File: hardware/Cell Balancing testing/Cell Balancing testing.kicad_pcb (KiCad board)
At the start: 2 copper layers, 27.9 x 48.8 mm, 29 parts, among them J1 pwm, J2 cell, U1 2PD2150-QX, U2 2PD2150-QX, U3 2PD2150-QX, U4 2PD2150-QX, U5 DMN62D0U

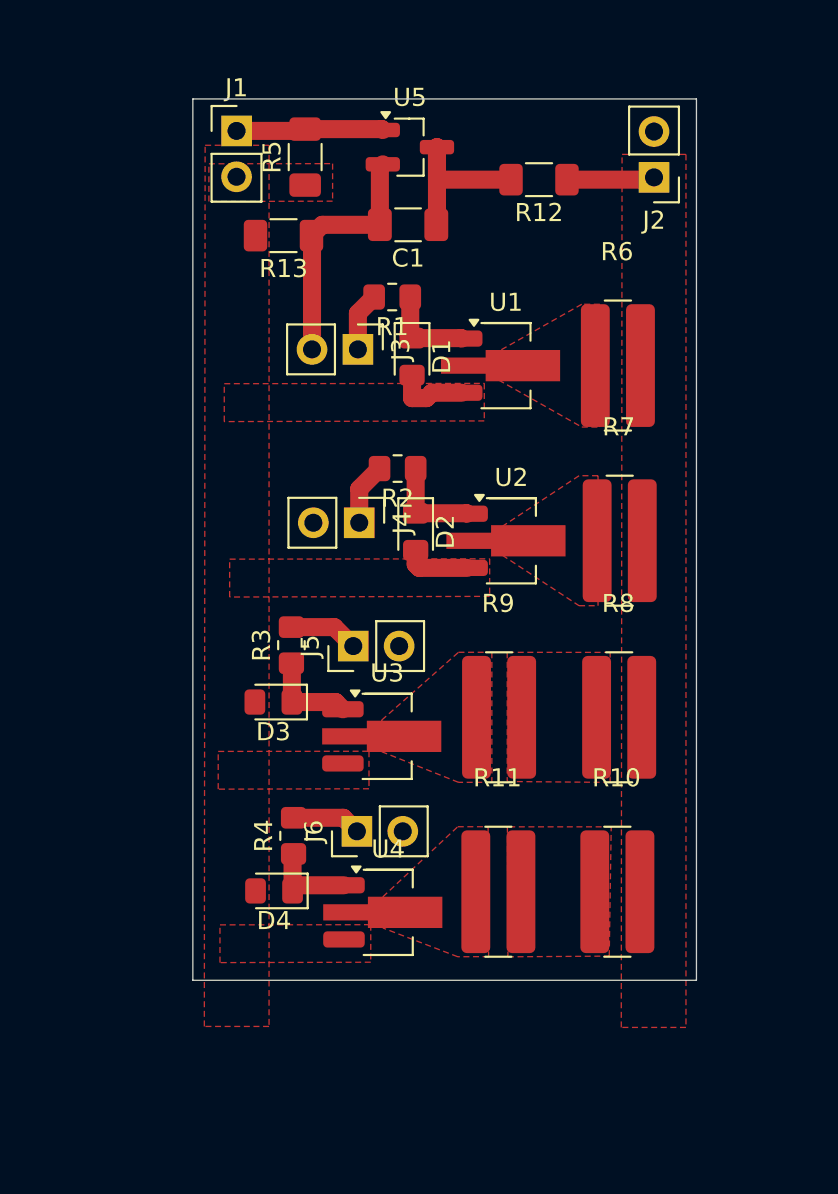
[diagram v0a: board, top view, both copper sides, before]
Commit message: VT interconnect cable specs and w5500 test board
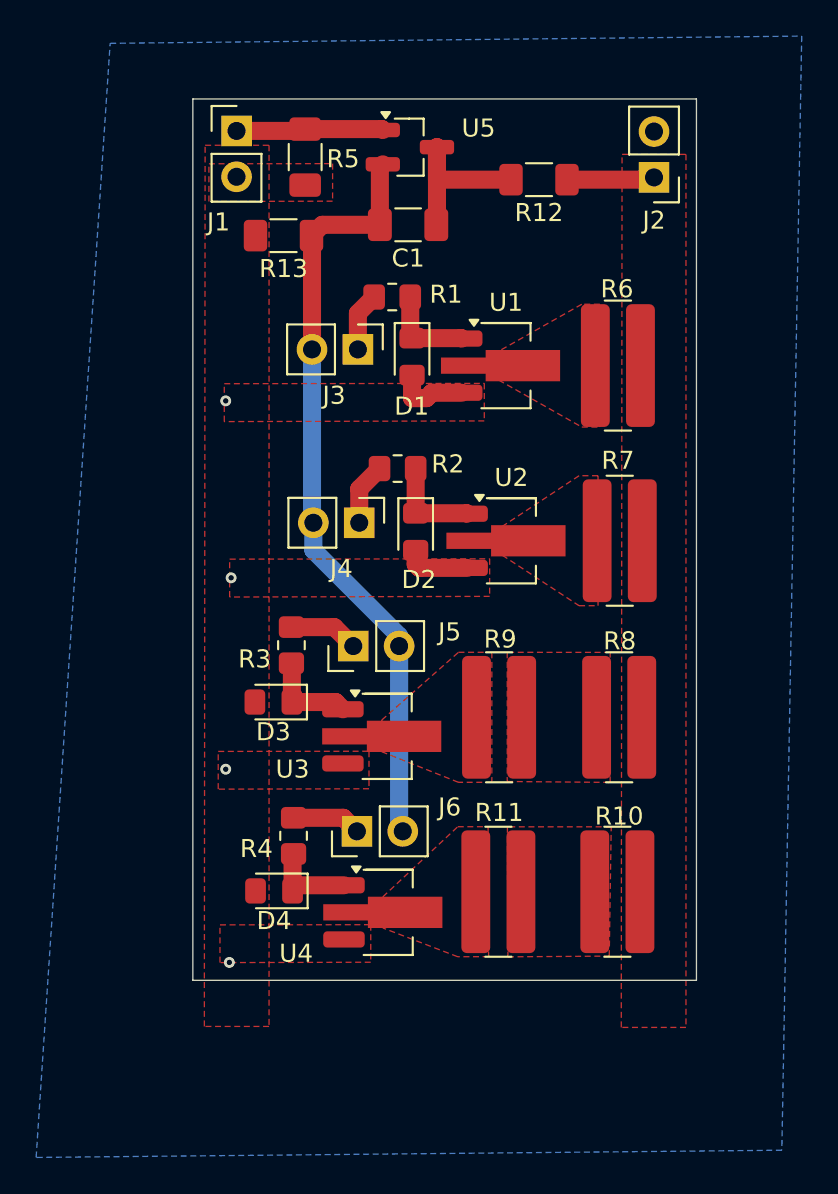
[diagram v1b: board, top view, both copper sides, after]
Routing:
- net /Rb: track 13.8 -> 42.5 mm
- net GND: vias 0 -> 4
- added copper zone on B.Cu, net GND
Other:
- board text added: "cell ballancing heating test"
- board text added: "gnd"
- board text added: "module+"
- board text added: "pwm"
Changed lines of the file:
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@@
 			(outputformat 1)
 			(mirror no)
-			(drillshape 1)
+			(drillshape 0)
 			(scaleselection 1)
-			(outputdirectory "")
+			(outputdirectory "C:/Users/turtl/Downloads/jlc/")
 		)
 	)
@@
 		(tags "Through hole pin header THT 1x02 2.54mm single row")
 		(property "Reference" "J1"
-			(at 0 -2.38 0)
+			(at -1 5.05 0)
 			(layer "F.SilkS")
 			(effects
@@
 		(at 103.54 87.025)
 		(property "Reference" "R8"
-			(at 0 -0.5 0)
+			(at 0.079999 1.575 0)
 			(unlocked yes)
 			(layer "F.SilkS")
@@
 		(tags "resistor handsolder")
 		(property "Reference" "R4"
-			(at 0 -1.65 90)
+			(at -0.709998 -2.057499 180)
 			(layer "F.SilkS")
 			(effects
@@
 		(at 96.85 96.685)
 		(property "Reference" "R11"
-			(at 0 -0.5 0)
+			(at 0.09 1.415 0)
 			(unlocked yes)
 			(layer "F.SilkS")
@@
 		(tags "resistor handsolder")
 		(property "Reference" "R5"
-			(at 0 -1.830001 90)
+			(at -0.1 2.1 180)
 			(layer "F.SilkS")
 			(effects
@@
 		(at 103.47 67.545)
 		(property "Reference" "R6"
-			(at -0.000002 -0.5 0)
+			(at 0 1.555 0)
 			(unlocked yes)
 			(layer "F.SilkS")
@@
 		(at 103.569999 77.245)
 		(property "Reference" "R7"
-			(at 0 -0.5 0)
+			(at -0.05 1.355 0)
 			(unlocked yes)
 			(layer "F.SilkS")
@@
 		(tags "resistor handsolder")
 		(property "Reference" "R3"
-			(at 0 -1.65 90)
+			(at -0.77 -2.04 180)
 			(layer "F.SilkS")
 			(effects
@@
 		(tags "diode handsolder")
 		(property "Reference" "D1"
-			(at 0 -1.65 90)
+			(at 2.75 0.019999 180)
 			(layer "F.SilkS")
 			(effects
@@
 		(tags "Through hole pin header THT 1x02 2.54mm single row")
 		(property "Reference" "J5"
-			(at 0 -2.38 90)
+			(at 0.78 5.334999 180)
 			(layer "F.SilkS")
 			(effects
@@
 		(at 103.44 96.685)
 		(property "Reference" "R10"
-			(at 0 -0.5 0)
+			(at 0.15 1.615 0)
 			(unlocked yes)
 			(layer "F.SilkS")
@@
 		(tags "SOT-89-3 Handsoldering")
 		(property "Reference" "U3"
-			(at -0.000002 -3.499999 0)
+			(at -5.24 1.82 0)
 			(layer "F.SilkS")
 			(effects
@@
 		(at 96.890001 87.025)
 		(property "Reference" "R9"
-			(at -0.000002 -0.5 0)
+			(at 0.109999 1.475 0)
 			(unlocked yes)
 			(layer "F.SilkS")
@@
 		(tags "resistor handsolder")
 		(property "Reference" "R2"
-			(at 0 -1.65 0)
+			(at -2.780001 0.25 0)
 			(layer "F.SilkS")
 			(effects
@@
 		(tags "Through hole pin header THT 1x02 2.54mm single row")
 		(property "Reference" "J6"
-			(at 0 -2.38 90)
+			(at 1.340001 5.135 180)
 			(layer "F.SilkS")
 			(effects
@@
 		(tags "SOT-89-3 Handsoldering")
 		(property "Reference" "U4"
-			(at 0 -3.5 0)
+			(at -5.099999 2.272499 0)
 			(layer "F.SilkS")
 			(effects
@@
 		(tags "Through hole pin header THT 1x02 2.54mm single row")
 		(property "Reference" "J3"
-			(at 0 -2.38 90)
+			(at 2.55 1.319999 180)
 			(layer "F.SilkS")
 			(effects
@@
 		(tags "SOT-23")
 		(property "Reference" "U5"
-			(at 0.000001 -2.75 0)
+			(at 3.8 -1.05 0)
 			(layer "F.SilkS")
 			(effects
@@
 		(tags "resistor handsolder")
 		(property "Reference" "R1"
-			(at 0 -1.65 0)
+			(at -2.980001 0.15 0)
 			(layer "F.SilkS")
 			(effects
@@
 		(tags "Through hole pin header THT 1x02 2.54mm single row")
 		(property "Reference" "J4"
-			(at 0 -2.38 90)
+			(at 2.55 0.994999 180)
 			(layer "F.SilkS")
 			(effects
@@
 		(tags "diode handsolder")
 		(property "Reference" "D2"
-			(at 0 -1.65 90)
+			(at 2.65 -0.180001 180)
 			(layer "F.SilkS")
 			(effects
@@
 		(layer "Edge.Cuts")
 	)
+	(gr_text "gnd"
+		(at 103.6 60.8 0)
+		(layer "B.SilkS")
+		(effects
+			(font
+				(size 1 1)
+				(thickness 0.1)
+			)
+			(justify left bottom mirror)
+		)
+	)
+	(gr_text "gnd"
+		(at 87.33 64.25 0)
+		(layer "B.SilkS")
+		(effects
+			(font
+				(size 1 1)
+				(thickness 0.1)
+			)
+			(justify left bottom mirror)
+		)
+	)
+	(gr_text "pwm"
+		(at 87.6 60.7 0)
+		(layer "B.SilkS")
+		(effects
+			(font
+				(size 1 1)
+				(thickness 0.1)
+			)
+			(justify left bottom mirror)
+		)
+	)
+	(gr_text "module+"
+		(at 103.9 63.5 0)
+		(layer "B.SilkS")
+		(effects
+			(font
+				(size 1 1)
+				(thickness 0.1)
+			)
+			(justify left bottom mirror)
+		)
+	)
+	(gr_text "cell ballancing heating test"
+		(at 104.3 68.1 0)
+		(layer "B.SilkS")
+		(effects
+			(font
+				(size 1 1)
+				(thickness 0.1)
+			)
+			(justify left bottom mirror)
+		)
+	)
 	(segment
 		(start 92.519999 84.55)
@@
 		(net 1)
 	)
+	(via
+		(at 81.8 95.7)
+		(size 0.6)
+		(drill 0.3)
+		(layers "F.Cu" "B.Cu")
+		(free yes)
+		(net 1)
+	)
+	(via
+		(at 82.1 85.1)
+		(size 0.6)
+		(drill 0.3)
+		(layers "F.Cu" "B.Cu")
+		(free yes)
+		(net 1)
+	)
+	(via
+		(at 81.8 75.3)
+		(size 0.6)
+		(drill 0.3)
+		(layers "F.Cu" "B.Cu")
+		(free yes)
+		(net 1)
+	)
+	(via
+		(at 82 106.4)
+		(size 0.6)
+		(drill 0.3)
+		(layers "F.Cu" "B.Cu")
+		(free yes)
+		(net 1)
+	)
 	(segment
 		(start 86.1 60.35)
@@
 	)
 	(segment
+		(start 86.579999 72.45)
+		(end 86.579999 81.975)
+		(width 1)
+		(layer "B.Cu")
+		(net 3)
+	)
+	(segment
+		(start 91.405001 88.88)
+		(end 91.405001 98.940002)
+		(width 1)
+		(layer "B.Cu")
+		(net 3)
+	)
+	(segment
+		(start 86.654999 82.05)
+		(end 86.654999 83.567998)
+		(width 1)
+		(layer "B.Cu")
+		(net 3)
+	)
+	(segment
+		(start 91.405001 88.318)
+		(end 91.405001 88.88)
+		(width 1)
+		(layer "B.Cu")
+		(net 3)
+	)
+	(segment
+		(start 86.654999 83.567998)
+		(end 91.405001 88.318)
+		(width 1)
+		(layer "B.Cu")
+		(net 3)
+	)
+	(segment
+		(start 91.405001 98.940002)
+		(end 91.605 99.140001)
+		(width 1)
+		(layer "B.Cu")
+		(net 3)
+	)
+	(segment
+		(start 86.579999 81.975)
+		(end 86.654999 82.05)
+		(width 1)
+		(layer "B.Cu")
+		(net 3)
+	)
+	(segment
 		(start 93.5 61.25)
 		(end 93.5 63.05)
@@
 			)
 		)
+	)
+	(zone
+		(net 1)
+		(net_name "GND")
+		(layer "B.Cu")
+		(hatch edge 0.5)
+		(priority 7)
+		(connect_pads yes
+			(clearance 0.5)
+		)
+		(min_thickness 0.25)
+		(filled_areas_thickness no)
+		(fill yes
+			(thermal_gap 0.5)
+			(thermal_bridge_width 0.5)
+		)
+		(polygon
+			(pts
+				(xy 75.4 55.5) (xy 113.7 55.1) (xy 112.6 116.8) (xy 71.3 117.2)
+			)
+		)
